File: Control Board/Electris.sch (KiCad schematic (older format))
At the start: 0 parts

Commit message: Complete schematic
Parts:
- added C1, C10, C2, C3, C7, C8, C9: 0.1uF, Capacitor_SMD:C_0603_1608Metric_Pad1.08x0.95mm_HandSolder, symbol Device:C
- added C11, C12, C4, C5: 18pF, Capacitor_SMD:C_0603_1608Metric_Pad1.08x0.95mm_HandSolder, symbol Device:C
- added C6: 47uF, Capacitor_THT:CP_Radial_D5.0mm_P2.50mm, symbol Device:CP1
- added D1: NSR0530HT1G, Diode_SMD:D_SOD-323_HandSoldering, symbol Device:D_Schottky
- added F1: 500mA, Fuse:Fuse_0603_1608Metric_Pad1.05x0.95mm_HandSolder, symbol Device:Fuse
- added FB1: Ferrite, Inductor_SMD:L_0603_1608Metric_Pad1.05x0.95mm_HandSolder, symbol Device:Ferrite_Bead_Small
- added J1: Barrel_Jack, Connector_BarrelJack:BarrelJack_Horizontal, symbol Connector:Barrel_Jack
- added J2: CTRL_ICSP, Connector_PinHeader_2.54mm:PinHeader_2x03_P2.54mm_Vertical, symbol Connector_Generic:Conn_02x03_Odd_Even
- added J3: GFX_ICSP, Connector_PinHeader_2.54mm:PinHeader_2x03_P2.54mm_Vertical, symbol Connector_Generic:Conn_02x03_Odd_Even
- added J4: VGA, jlib:Connector_Amphenol_ICD15S13E4GX00LF, symbol Connector:DB15_Female
- added JP1: CTRL_RST, Jumper:SolderJumper-2_P1.3mm_Open_RoundedPad1.0x1.5mm, symbol Device:Jumper_NC_Small
- added JP2: GFX_RST, Jumper:SolderJumper-2_P1.3mm_Open_RoundedPad1.0x1.5mm, symbol Device:Jumper_NC_Small
- added JP3: 6R, Jumper:SolderJumper-2_P1.3mm_Open_RoundedPad1.0x1.5mm, symbol Device:Jumper_NC_Small
- added JP4: 6G, Jumper:SolderJumper-2_P1.3mm_Open_RoundedPad1.0x1.5mm, symbol Device:Jumper_NC_Small
- added JP5: 6B, Jumper:SolderJumper-2_P1.3mm_Open_RoundedPad1.0x1.5mm, symbol Device:Jumper_NO_Small
- added JP6: 7R, Jumper:SolderJumper-2_P1.3mm_Open_RoundedPad1.0x1.5mm, symbol Device:Jumper_NO_Small
- added JP7: 7G, Jumper:SolderJumper-2_P1.3mm_Open_RoundedPad1.0x1.5mm, symbol Device:Jumper_NO_Small
- added JP8: 7B, Jumper:SolderJumper-2_P1.3mm_Open_RoundedPad1.0x1.5mm, symbol Device:Jumper_NC_Small
- added JP9: TONE, Jumper:SolderJumper-3_P1.3mm_Open_RoundedPad1.0x1.5mm_NumberLabels, symbol Jumper:Jumper_3_Open
- added L1: 47uH, Inductor_SMD:L_1210_3225Metric_Pad1.42x2.65mm_HandSolder, symbol Device:L
- added LS1: Speaker, Connector_PinHeader_2.54mm:PinHeader_1x02_P2.54mm_Vertical, symbol Device:Speaker
- added Q1: MMBT2222ALT3G, Package_TO_SOT_SMD:SOT-23_Handsoldering, symbol Device:Q_NPN_BEC
- added R1, R10, R11, R12, R13, R14, R2, R8, R9: 10K, Resistor_SMD:R_0603_1608Metric_Pad0.98x0.95mm_HandSolder, symbol Device:R_US
- added R3, R4: 68, Resistor_SMD:R_0805_2012Metric_Pad1.20x1.40mm_HandSolder, symbol Device:R_US
- added R5, R6: 470, Resistor_SMD:R_0603_1608Metric_Pad0.98x0.95mm_HandSolder, symbol Device:R_US
- added R7: 1K, Resistor_SMD:R_0603_1608Metric_Pad0.98x0.95mm_HandSolder, symbol Device:R_US
- added SW1: SW_ML, Button_Switch_THT:SW_PUSH-12mm, symbol Switch:SW_Push
- added SW2: SW_MR, Button_Switch_THT:SW_PUSH-12mm, symbol Switch:SW_Push
- added SW3: SW_TL, Button_Switch_THT:SW_PUSH-12mm, symbol Switch:SW_Push
- added SW4: SW_TR, Button_Switch_THT:SW_PUSH-12mm, symbol Switch:SW_Push
- added SW5: SW_DS, Button_Switch_THT:SW_PUSH-12mm, symbol Switch:SW_Push
- added SW6: SW_DH, Button_Switch_THT:SW_PUSH-12mm, symbol Switch:SW_Push
- added SW7: SW_HL, Button_Switch_THT:SW_PUSH-12mm, symbol Switch:SW_Push
- added U1, U3: ATmega328P-AU, Package_QFP:TQFP-32_7x7mm_P0.8mm, symbol MCU_Microchip_ATmega:ATmega328P-AU
- added U2: AP1509-50SG-13, Package_SO:SOP-8_3.9x4.9mm_P1.27mm, symbol jlib:AP1509-50SG-13
- added Y1, Y2: 16MHz, Crystal:Crystal_HC49-4H_Vertical, symbol Device:Crystal
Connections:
- new net: C4.2, U1.7 (XTAL1/PB6), Y1.1
- new net: C5.2, U1.8 (XTAL2/PB7), Y1.2
- new net: C2.1, U1.20 (AREF)
- new net: D1.1 (K), L1.1, U2.2 (OUT)
- new net: C6.1, C7.1, FB1.2, L1.2
- new net: R4.2, U3.1 (PD3)
- new net: R5.2, U3.10 (PD6)
- new net: R6.2, U3.11 (PD7)
- new net: R3.2, U3.13 (PB1)
- new net: C9.1, U3.20 (AREF)
- new net: C11.2, U3.7 (XTAL1/PB6), Y2.1
- new net: C12.2, U3.8 (XTAL2/PB7), Y2.2
- new net: Q1.1 (B), R7.1
- new net: LS1.2, Q1.3 (C)
- new net: JP3.1, JP4.1, JP5.1, R5.1
- new net: JP6.1, JP7.1, JP8.1, R6.1
- new net: F1.2, J1.1
- new net +12V: C3.1, F1.1, U2.1 (VIN)
- new net +5V: C1.1, C10.1, C8.1, FB1.1, J2.2 (Pin_2), J3.2 (Pin_2), LS1.1, R1.1, R2.1, SW1.2, SW2.2, SW3.2, SW4.2, SW5.2, SW6.2, SW7.2, U1.18 (AVCC), U1.4 (VCC), U1.6 (VCC), U2.3 (FB), U3.18 (AVCC), U3.4 (VCC), U3.6 (VCC)
- new net BTN_DH: R13.1, SW6.1, U1.11 (PD7)
- new net BTN_DS: R12.1, SW5.1, U1.10 (PD6)
- new net BTN_HL: R14.1, SW7.1, U1.28 (PC5)
- new net BTN_ML: R8.1, SW1.1, U1.32 (PD2)
- new net BTN_MR: R9.1, SW2.1, U1.1 (PD3)
- new net BTN_TL: R10.1, SW3.1, U1.2 (PD4)
- new net BTN_TR: R11.1, SW4.1, U1.9 (PD5)
- new net GND: C1.2, C10.2, C11.1, C12.1, C2.2, C3.2, C4.1, C5.1, C6.2, C7.2, C8.2, C9.2, D1.2 (A), J1.2, J2.6 (Pin_6), J3.6 (Pin_6), J4.10 (P10), J4.5, J4.6, J4.7, J4.8, JP1.1, JP2.1, Q1.2 (E), R10.2, R11.2, R12.2, R13.2, R14.2, R8.2, R9.2, U1.21 (GND), U1.3 (GND), U1.5 (GND), U2.4 (SD), U2.5 (GND), U2.6 (GND), U2.7 (GND), U2.8 (GND), U3.21 (GND), U3.3 (GND), U3.5 (GND)
- new net ICSP_MISO_1: J2.1 (Pin_1), U1.16 (PB4)
- new net ICSP_MISO_2: J3.1 (Pin_1), U3.16 (PB4)
- new net ICSP_MOSI_1: J2.4 (Pin_4), U1.15 (PB3)
- new net ICSP_MOSI_2: J3.4 (Pin_4), U3.15 (PB3)
- new net ICSP_SCK_1: J2.3 (Pin_3), U1.17 (PB5)
- new net ICSP_SCK_2: J3.3 (Pin_3), U3.17 (PB5)
- new net TONE: JP9.2 (C), R7.2
- new net TONE_1: JP9.3 (B), U1.13 (PB1)
- new net TONE_2: JP9.1 (A), U3.14 (PB2)
- new net UART_RX: U1.30 (PD0), U3.30 (PD0)
- new net UART_TX: U1.31 (PD1), U3.31 (PD1)
- new net VGA_B: J4.3, JP5.2, JP8.2
- new net VGA_G: J4.2, JP4.2, JP7.2
- new net VGA_HSYNC: J4.13 (P13), R4.1
- new net VGA_R: J4.1, JP3.2, JP6.2
- new net VGA_VSYNC: J4.14 (P14), R3.1
- new net nRST_1: J2.5 (Pin_5), JP1.2, R1.2, U1.29 (~RESET~/PC6)
- new net nRST_2: J3.5 (Pin_5), JP2.2, R2.2, U3.29 (~RESET~/PC6)
- no-connect marks 0 -> 26

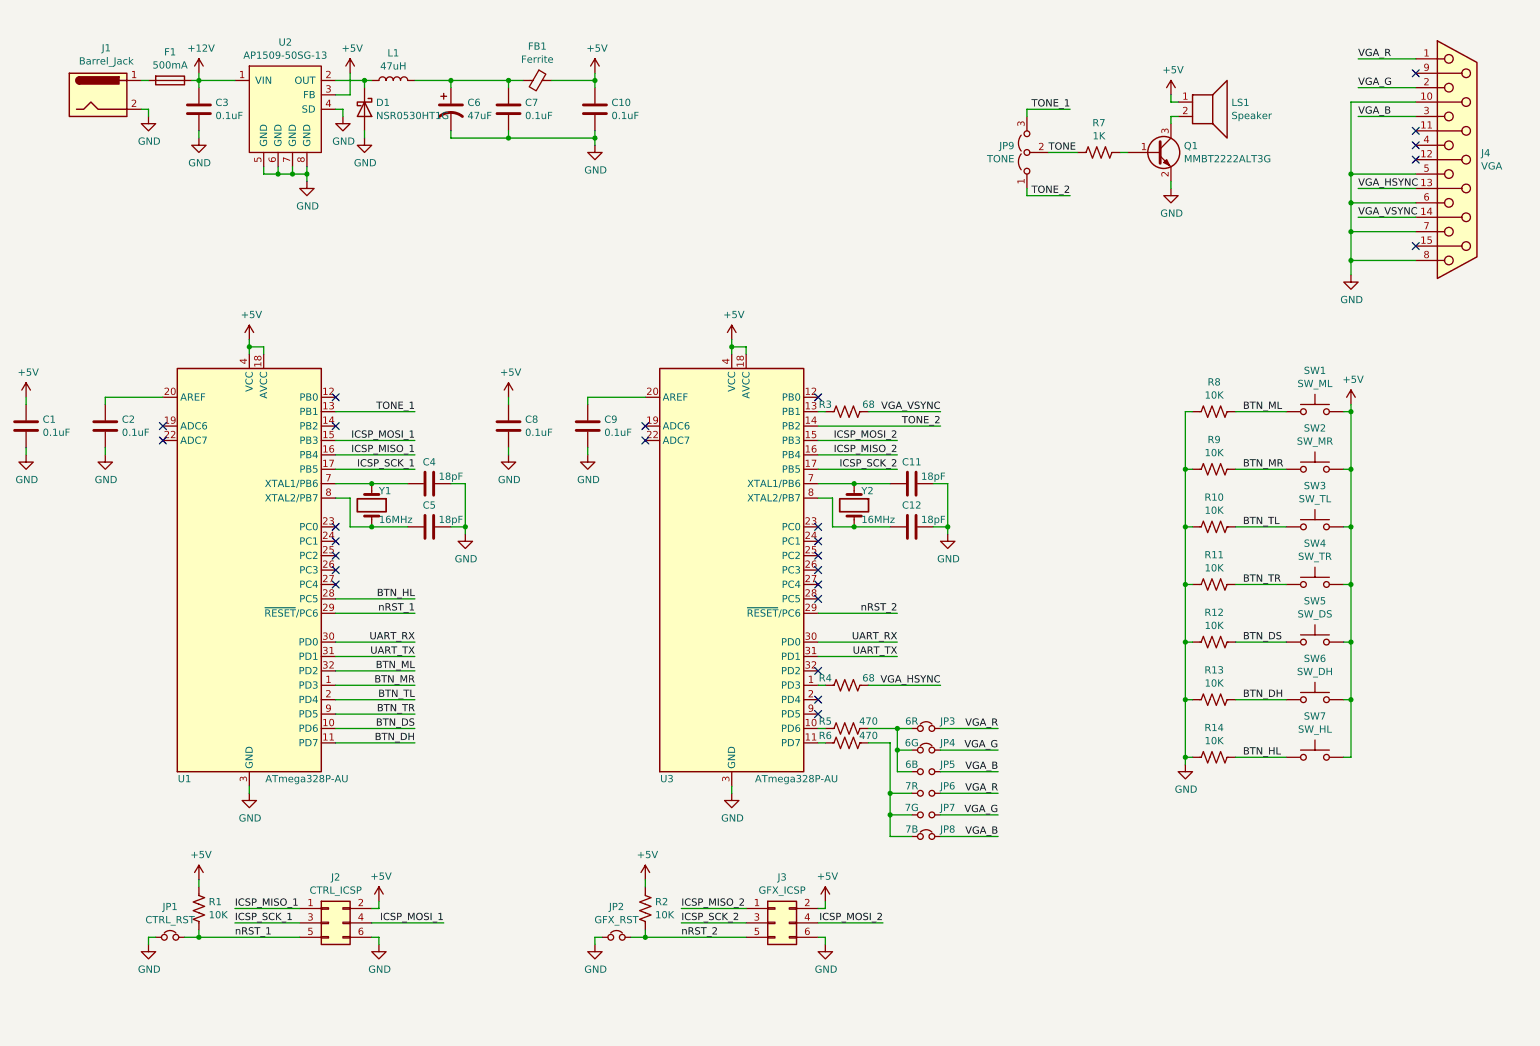
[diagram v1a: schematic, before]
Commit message: Switched to RP2040, finished schematic, started layout.
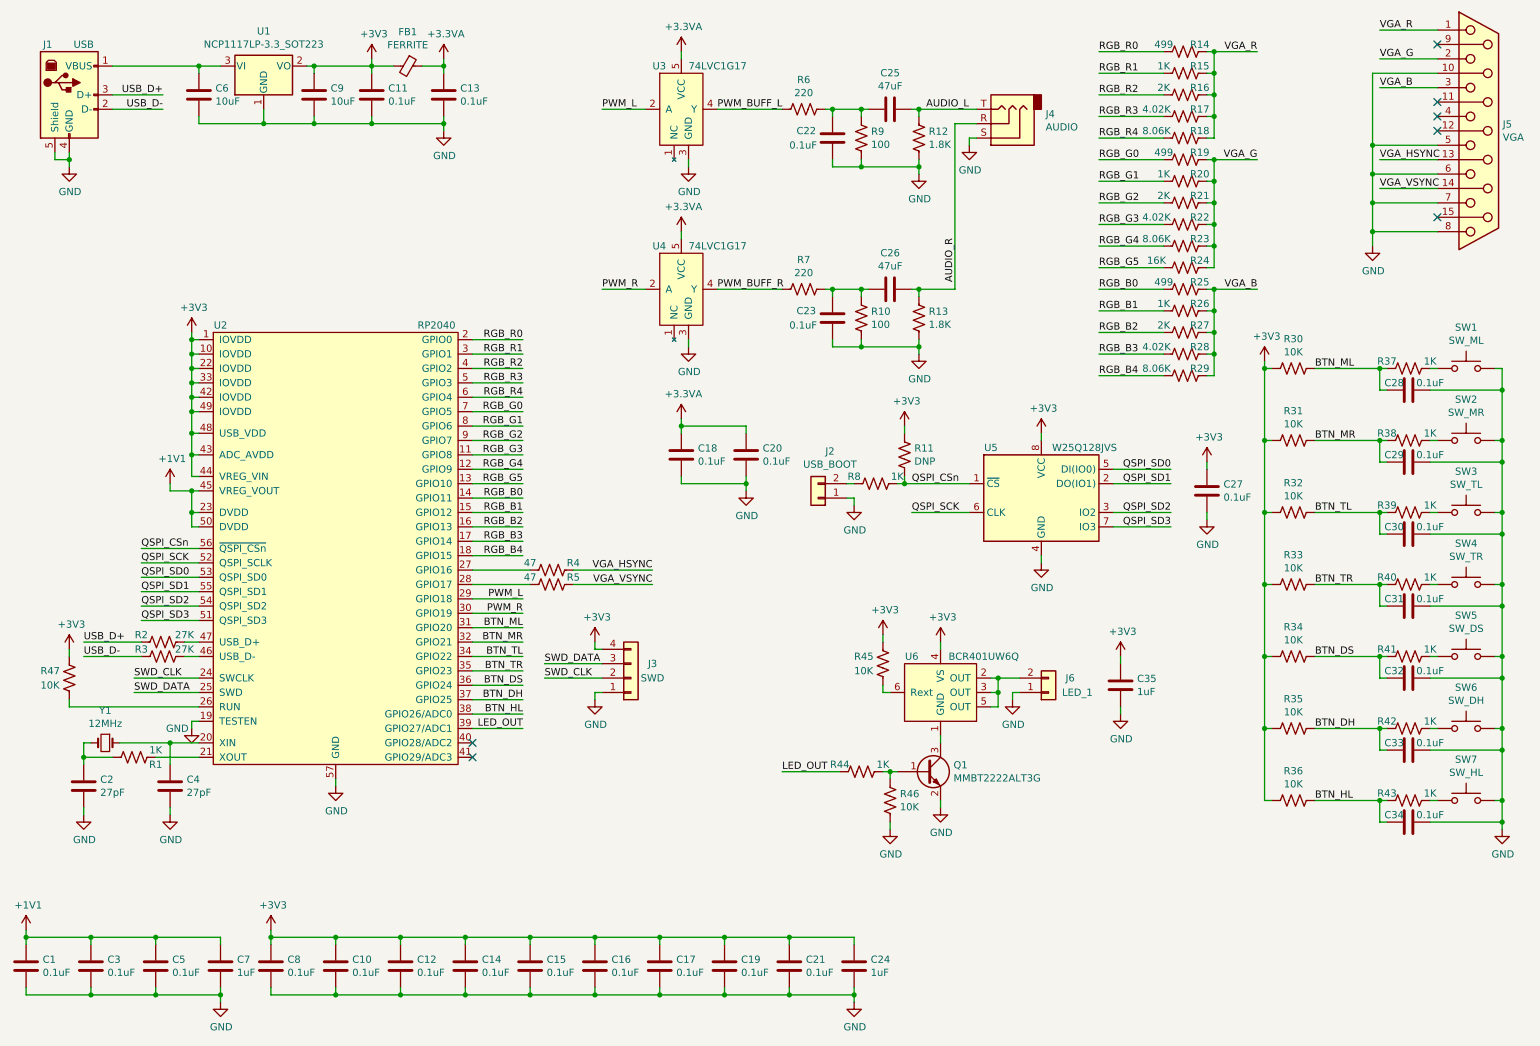
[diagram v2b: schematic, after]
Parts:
- removed C6: 47uF, Capacitor_THT:CP_Radial_D5.0mm_P2.50mm, symbol Device:CP1
- removed D1: NSR0530HT1G, Diode_SMD:D_SOD-323_HandSoldering, symbol Device:D_Schottky
- removed F1: 500mA, Fuse:Fuse_0603_1608Metric_Pad1.05x0.95mm_HandSolder, symbol Device:Fuse
- removed J1: Barrel_Jack, Connector_BarrelJack:BarrelJack_Horizontal, symbol Connector:Barrel_Jack
- removed J2: CTRL_ICSP, Connector_PinHeader_2.54mm:PinHeader_2x03_P2.54mm_Vertical, symbol Connector_Generic:Conn_02x03_Odd_Even
- removed J3: GFX_ICSP, Connector_PinHeader_2.54mm:PinHeader_2x03_P2.54mm_Vertical, symbol Connector_Generic:Conn_02x03_Odd_Even
- removed JP1: CTRL_RST, Jumper:SolderJumper-2_P1.3mm_Open_RoundedPad1.0x1.5mm, symbol Device:Jumper_NC_Small
- removed JP2: GFX_RST, Jumper:SolderJumper-2_P1.3mm_Open_RoundedPad1.0x1.5mm, symbol Device:Jumper_NC_Small
- removed JP3: 6R, Jumper:SolderJumper-2_P1.3mm_Open_RoundedPad1.0x1.5mm, symbol Device:Jumper_NC_Small
- removed JP4: 6G, Jumper:SolderJumper-2_P1.3mm_Open_RoundedPad1.0x1.5mm, symbol Device:Jumper_NC_Small
- removed JP5: 6B, Jumper:SolderJumper-2_P1.3mm_Open_RoundedPad1.0x1.5mm, symbol Device:Jumper_NO_Small
- removed JP6: 7R, Jumper:SolderJumper-2_P1.3mm_Open_RoundedPad1.0x1.5mm, symbol Device:Jumper_NO_Small
- removed JP7: 7G, Jumper:SolderJumper-2_P1.3mm_Open_RoundedPad1.0x1.5mm, symbol Device:Jumper_NO_Small
- removed JP8: 7B, Jumper:SolderJumper-2_P1.3mm_Open_RoundedPad1.0x1.5mm, symbol Device:Jumper_NC_Small
- removed JP9: TONE, Jumper:SolderJumper-3_P1.3mm_Open_RoundedPad1.0x1.5mm_NumberLabels, symbol Jumper:Jumper_3_Open
- removed L1: 47uH, Inductor_SMD:L_1210_3225Metric_Pad1.42x2.65mm_HandSolder, symbol Device:L
- removed LS1: Speaker, Connector_PinHeader_2.54mm:PinHeader_1x02_P2.54mm_Vertical, symbol Device:Speaker
- removed U1, U3: ATmega328P-AU, Package_QFP:TQFP-32_7x7mm_P0.8mm, symbol MCU_Microchip_ATmega:ATmega328P-AU
- removed U2: AP1509-50SG-13, Package_SO:SOP-8_3.9x4.9mm_P1.27mm, symbol jlib:AP1509-50SG-13
- removed Y1, Y2: 16MHz, Crystal:Crystal_HC49-4H_Vertical, symbol Device:Crystal
- added C13, C14, C15, C16, C17, C18, C19, C20, C21, C22, C23, C27, C28, C29, C30, C31, C32, C33, C34: 0.1uF, Capacitor_SMD:C_0603_1608Metric_Pad1.08x0.95mm_HandSolder, symbol Device:C
- added C24, C35: 1uF, Capacitor_SMD:C_0603_1608Metric_Pad1.08x0.95mm_HandSolder, symbol Device:C
- added C25, C26: 47uF, Capacitor_SMD:C_0805_2012Metric_Pad1.18x1.45mm_HandSolder, symbol Device:C
- added C6: 10uF, Capacitor_SMD:C_0805_2012Metric_Pad1.18x1.45mm_HandSolder, symbol Device:C
- added J1: USB, Connector_USB:USB_B_OST_USB-B1HSxx_Horizontal, symbol Connector:USB_B
- added J2: USB_BOOT, Jumper:SolderJumper-2_P1.3mm_Open_RoundedPad1.0x1.5mm, symbol Connector_Generic:Conn_01x02
- added J3: SWD, Connector_PinHeader_2.54mm:PinHeader_1x04_P2.54mm_Vertical, symbol Connector_Generic:Conn_01x04
- added J4: AUDIO, jlib:Connector_CUI_SJ1-2503A, symbol Connector:AudioJack3
- added J6: LED_1, Connector_JST:JST_EH_B2B-EH-A_1x02_P2.50mm_Vertical, symbol Connector_Generic:Conn_01x02
- added R10, R9: 100, Resistor_SMD:R_0805_2012Metric_Pad1.20x1.40mm_HandSolder, symbol Device:R_US
- added R11: DNP, Resistor_SMD:R_0603_1608Metric_Pad0.98x0.95mm_HandSolder, symbol Device:R_US
- added R12, R13: 1.8K, Resistor_SMD:R_0805_2012Metric_Pad1.20x1.40mm_HandSolder, symbol Device:R_US
- added R14, R19, R25: 499, Resistor_SMD:R_0603_1608Metric_Pad0.98x0.95mm_HandSolder, symbol Device:R_US
- added R15, R20, R26, R37, R38, R39, R40, R41, R42, R43, R44, R8: 1K, Resistor_SMD:R_0603_1608Metric_Pad0.98x0.95mm_HandSolder, symbol Device:R_US
- added R16, R21, R27: 2K, Resistor_SMD:R_0603_1608Metric_Pad0.98x0.95mm_HandSolder, symbol Device:R_US
- added R17, R22, R28: 4.02K, Resistor_SMD:R_0603_1608Metric_Pad0.98x0.95mm_HandSolder, symbol Device:R_US
- added R18, R23, R29: 8.06K, Resistor_SMD:R_0603_1608Metric_Pad0.98x0.95mm_HandSolder, symbol Device:R_US
- added R24: 16K, Resistor_SMD:R_0603_1608Metric_Pad0.98x0.95mm_HandSolder, symbol Device:R_US
- added R45, R46, R47: 10K, Resistor_SMD:R_0603_1608Metric_Pad0.98x0.95mm_HandSolder, symbol Device:R_US
- added U1: NCP1117LP-3.3_SOT223, Package_TO_SOT_SMD:SOT-223-3_TabPin2, symbol Regulator_Linear:NCP1117-3.3_SOT223
- added U2: RP2040, jlib:QFN_RP2040, symbol jlib:RP2040
- added U3, U4: 74LVC1G17, Package_TO_SOT_SMD:TSOT-23-5_HandSoldering, symbol jlib:74LVC1G17
- added U5: W25Q128JVS, Package_SO:SOIC-8_5.23x5.23mm_P1.27mm, symbol Memory_Flash:W25Q128JVS
- added U6: BCR401UW6Q, Package_TO_SOT_SMD:SOT-23-6_Handsoldering, symbol jlib:BCR401UW6Q
- added Y1: 12MHz, Crystal:Crystal_SMD_HC49-SD, symbol Device:Crystal_Small
- C11, C12, C5: value 18pF -> 0.1uF
- C2: value 0.1uF -> 27pF
- C4: value 18pF -> 27pF
- C7: value 0.1uF -> 1uF
- C9: value 0.1uF -> 10uF; footprint Capacitor_SMD:C_0603_1608Metric_Pad1.08x0.95mm_HandSolder -> Capacitor_SMD:C_0805_2012Metric_Pad1.18x1.45mm_HandSolder
- FB1: value Ferrite -> FERRITE
- Q1: footprint Package_TO_SOT_SMD:SOT-23_Handsoldering -> Package_TO_SOT_SMD:TSOT-23_HandSoldering
- R1: value 10K -> 1K
- R2: value 10K -> 27K; footprint Resistor_SMD:R_0603_1608Metric_Pad0.98x0.95mm_HandSolder -> Resistor_SMD:R_0805_2012Metric_Pad1.20x1.40mm_HandSolder
- R3: value 68 -> 27K
- R4: value 68 -> 47; footprint Resistor_SMD:R_0805_2012Metric_Pad1.20x1.40mm_HandSolder -> Resistor_SMD:R_0603_1608Metric_Pad0.98x0.95mm_HandSolder
- R5: value 470 -> 47
- R6: value 470 -> 220; footprint Resistor_SMD:R_0603_1608Metric_Pad0.98x0.95mm_HandSolder -> Resistor_SMD:R_0805_2012Metric_Pad1.20x1.40mm_HandSolder
- R7: value 1K -> 220; footprint Resistor_SMD:R_0603_1608Metric_Pad0.98x0.95mm_HandSolder -> Resistor_SMD:R_0805_2012Metric_Pad1.20x1.40mm_HandSolder
- SW1, SW2, SW3, SW4, SW5, SW6, SW7: footprint Button_Switch_THT:SW_PUSH-12mm -> Connector_JST:JST_EH_B2B-EH-A_1x02_P2.50mm_Vertical
- renumbered J4 to J5, R8 to R30, R9 to R31, R10 to R32, R11 to R33, R12 to R34, R13 to R35, R14 to R36
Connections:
- net +12V is gone; now on net +1V1: C3.1
- net nRST_1 is gone; now on an unnamed net: R1.2
- net BTN_DH: now also C33.2, R42.2, U2.37 (GPIO25); no longer SW6.1
- net BTN_DS: now also C32.2, R41.2, U2.36 (GPIO24); no longer SW5.1
- net BTN_HL: now also C34.2, R43.2, U2.38 (GPIO26/ADC0); no longer SW7.1
- net BTN_ML: now also C28.2, R37.2, U2.31 (GPIO20); no longer SW1.1
- net BTN_MR: now also C29.2, R38.2, U2.32 (GPIO21); no longer SW2.1
- net BTN_TL: now also C30.2, R39.2, U2.34 (GPIO22); no longer SW3.1
- net BTN_TR: now also C31.2, R40.2, U2.35 (GPIO23); no longer SW4.1
- net GND: now also C11.2, C12.2, C4.2, C5.2, SW1.2, SW2.2, SW3.2, SW4.2, SW5.2, SW6.2, SW7.2, C13.2, C14.2, C15.2, C16.2, C17.2, C18.2, C19.2, C20.2, C21.2, C22.2, C23.2, C24.2, C27.2, C28.1, C29.1, C30.1, C31.1, C32.1, C33.1, C34.1, C35.2, C6.2, J1.4 (GND), J1.5 (Shield), J2.1 (Pin_1), J3.1 (Pin_1), J4.S, J6.1 (Pin_1), R10.2, R12.2, R13.2, R46.2, R9.2, U1.1 (GND), U2.19 (TESTEN), U2.57 (GND), U3.3 (GND), U4.3 (GND), U5.4 (GND); no longer C11.1, C12.1, C4.1, C5.1, R30.2, R31.2, R32.2, R33.2, R34.2, R35.2, R36.2
- net VGA_B: now also R25.1, R26.1, R27.1, R28.1, R29.1
- net VGA_G: now also R19.1, R20.1, R21.1, R22.1, R23.1, R24.1
- net VGA_R: now also R14.1, R15.1, R16.1, R17.1, R18.1
- net VGA_VSYNC: now also R5.1; no longer R3.1
- net at C2.1: now also Y1.2
- net +1V1: now reaches C7.1
- net +1V1: now also C1.1, C5.1, U2.23 (DVDD), U2.45 (VREG_VOUT), U2.50 (DVDD); no longer FB1.2
- net at R4.2: now also U2.27 (GPIO16)
- net at R5.2: now also U2.28 (GPIO17)
- net PWM_BUFF_L: now reaches R6.2
- net PWM_BUFF_L: now also U3.4 (Y)
- net USB_D-: now reaches R3.2
- net USB_D-: now also J1.2 (D-)
- net +3V3: now reaches C9.1
- net +3V3: now also C10.1, C11.1, C12.1, C8.1, FB1.2, R30.2, R31.2, R32.2, R33.2, R34.2, R35.2, R36.2, C14.1, C15.1, C16.1, C17.1, C19.1, C21.1, C24.1, C27.1, C35.1, J3.4 (Pin_4), R11.1, R45.1, R47.1, U1.2 (VO), U2.1 (IOVDD), U2.10 (IOVDD), U2.22 (IOVDD), U2.33 (IOVDD), U2.42 (IOVDD), U2.43 (ADC_AVDD), U2.44 (VREG_VIN), U2.48 (USB_VDD), U2.49 (IOVDD), U5.8 (VCC), U6.4 (VS)
- net at Q1.1 (B): now also R44.1, R46.1; no longer R7.1
- net at Q1.3 (C): now also U6.1 (GND)
- net at R6.1: now also C22.1, C25.2, R9.1
- removed net +5V: C1.1, C10.1, C8.1, FB1.1, R1.1, R2.1, SW1.2, SW2.2, SW3.2, SW4.2, SW5.2, SW6.2, SW7.2
- net TONE renamed PWM_BUFF_R
- net PWM_BUFF_R: now also U4.4 (Y)
- net nRST_2 renamed USB_D+
- net USB_D+: now also J1.3 (D+)
- new net: R40.1, SW4.1
- new net: R41.1, SW5.1
- new net: R42.1, SW6.1
- new net: R43.1, SW7.1
- new net: R37.1, SW1.1
- new net: R38.1, SW2.1
- new net: R39.1, SW3.1
- new net: C4.1, U2.20 (XIN), Y1.1
- new net: R1.1, U2.21 (XOUT)
- new net: R47.2, U2.26 (RUN)
- new net: R3.1, U2.46 (USB_D-)
- new net: R2.1, U2.47 (USB_D+)
- new net: J6.2 (Pin_2), U6.2 (OUT), U6.3 (OUT), U6.5 (OUT)
- new net: R45.2, U6.6 (Rext)
- new net: J2.2 (Pin_2), R8.2
- new net: C6.1, J1.1 (VBUS), U1.3 (VI)
- new net: C23.1, C26.2, R10.1, R7.1
- new net +3.3VA: C13.1, C18.1, C20.1, FB1.1, U3.5 (VCC), U4.5 (VCC)
- new net AUDIO_L: C25.1, J4.T, R12.1
- new net AUDIO_R: C26.1, J4.R, R13.1
- new net LED_OUT: R44.2, U2.39 (GPIO27/ADC1)
- new net PWM_L: U2.29 (GPIO18), U3.2 (A)
- new net PWM_R: U2.30 (GPIO19), U4.2 (A)
- new net QSPI_CSn: R11.2, R8.1, U2.56 (~QSPI_CSn~), U5.1 (~CS)
- new net QSPI_SCK: U2.52 (QSPI_SCLK), U5.6 (CLK)
- new net QSPI_SD0: U2.53 (QSPI_SD0), U5.5 (DI(IO0))
- new net QSPI_SD1: U2.55 (QSPI_SD1), U5.2 (DO(IO1))
- new net QSPI_SD2: U2.54 (QSPI_SD2), U5.3 (IO2)
- new net QSPI_SD3: U2.51 (QSPI_SD3), U5.7 (IO3)
- new net RGB_B0: R25.2, U2.14 (GPIO11)
- new net RGB_B1: R26.2, U2.15 (GPIO12)
- new net RGB_B2: R27.2, U2.16 (GPIO13)
- new net RGB_B3: R28.2, U2.17 (GPIO14)
- new net RGB_B4: R29.2, U2.18 (GPIO15)
- new net RGB_G0: R19.2, U2.7 (GPIO5)
- new net RGB_G1: R20.2, U2.8 (GPIO6)
- new net RGB_G2: R21.2, U2.9 (GPIO7)
- new net RGB_G3: R22.2, U2.11 (GPIO8)
- new net RGB_G4: R23.2, U2.12 (GPIO9)
- new net RGB_G5: R24.2, U2.13 (GPIO10)
- new net RGB_R0: R14.2, U2.2 (GPIO0)
- new net RGB_R1: R15.2, U2.3 (GPIO1)
- new net RGB_R2: R16.2, U2.4 (GPIO2)
- new net RGB_R3: R17.2, U2.5 (GPIO3)
- new net RGB_R4: R18.2, U2.6 (GPIO4)
- new net SWD_CLK: J3.2 (Pin_2), U2.24 (SWCLK)
- new net SWD_DATA: J3.3 (Pin_3), U2.25 (SWD)
- no-connect marks 26 -> 7
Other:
- moved on the sheet: J5, R30, R31, R32, R33, R34, R35, R36, SW1, SW2, SW3, SW4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

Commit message: Routing
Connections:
- net D-: now reaches R3.1, U2.46 (USB_D-)
- net D+: now reaches R2.1, U2.47 (USB_D+)
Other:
- moved on the sheet: R2, R3, R47
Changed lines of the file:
@@
 Text Label 7150 2450 1    50   ~ 0
 AUDIO_R
-Text Label 1450 5200 0    50   ~ 0
+Text Label 1300 5200 0    50   ~ 0
 SWD_CLK
 Wire Wire Line
-	1450 5200 1900 5200
-Wire Wire Line
-	1450 5300 1900 5300
-Text Label 1450 5300 0    50   ~ 0
+	1300 5200 1900 5200
+Wire Wire Line
+	1300 5300 1900 5300
+Text Label 1300 5300 0    50   ~ 0
 SWD_DATA
 $Comp
@@
 L Device:R_US R2
 U 1 1 614243B8
-P 1650 4950
-F 0 "R2" V 1600 4800 50  0000 C CNN
-F 1 "27K" V 1600 5100 50  0000 C CNN
-F 2 "Resistor_SMD:R_0805_2012Metric_Pad1.20x1.40mm_HandSolder" V 1690 4940 50  0001 C CNN
-F 3 "~" H 1650 4950 50  0001 C CNN
-	1    1650 4950
-	0    1    1    0
-$EndComp
-Wire Wire Line
-	1800 4950 1900 4950
-Wire Wire Line
-	1900 5050 1800 5050
+P 1500 4950
+F 0 "R2" V 1450 4800 50  0000 C CNN
+F 1 "27K" V 1450 5100 50  0000 C CNN
+F 2 "Resistor_SMD:R_0805_2012Metric_Pad1.20x1.40mm_HandSolder" V 1540 4940 50  0001 C CNN
+F 3 "~" H 1500 4950 50  0001 C CNN
+	1    1500 4950
+	0    1    1    0
+$EndComp
+Wire Wire Line
+	1650 4950 1900 4950
+Wire Wire Line
+	1900 5050 1650 5050
 $Comp
 L Device:R_US R3
 U 1 1 61459653
-P 1650 5050
-F 0 "R3" V 1600 4900 50  0000 C CNN
-F 1 "27K" V 1600 5200 50  0000 C CNN
-F 2 "Resistor_SMD:R_0805_2012Metric_Pad1.20x1.40mm_HandSolder" V 1690 5040 50  0001 C CNN
-F 3 "~" H 1650 5050 50  0001 C CNN
-	1    1650 5050
-	0    1    1    0
-$EndComp
-Wire Wire Line
-	1500 4950 1100 4950
-Wire Wire Line
-	1100 5050 1500 5050
-Text Label 1100 4950 0    50   ~ 0
+P 1500 5050
+F 0 "R3" V 1450 4900 50  0000 C CNN
+F 1 "27K" V 1450 5200 50  0000 C CNN
+F 2 "Resistor_SMD:R_0805_2012Metric_Pad1.20x1.40mm_HandSolder" V 1540 5040 50  0001 C CNN
+F 3 "~" H 1500 5050 50  0001 C CNN
+	1    1500 5050
+	0    1    1    0
+$EndComp
+Wire Wire Line
+	1350 4950 950  4950
+Wire Wire Line
+	950  5050 1350 5050
+Text Label 950  4950 0    50   ~ 0
 USB_D+
-Text Label 1100 5050 0    50   ~ 0
+Text Label 950  5050 0    50   ~ 0
 USB_D-
 $Comp
@@
 L Device:R_US R47
 U 1 1 61BCC099
-P 1000 5200
-F 0 "R47" H 800 5250 50  0000 L CNN
-F 1 "10K" H 800 5150 50  0000 L CNN
-F 2 "Resistor_SMD:R_0603_1608Metric_Pad0.98x0.95mm_HandSolder" V 1040 5190 50  0001 C CNN
-F 3 "~" H 1000 5200 50  0001 C CNN
-	1    1000 5200
-	1    0    0    -1
-$EndComp
-Wire Wire Line
-	1900 5400 1000 5400
-Wire Wire Line
-	1000 5400 1000 5350
-Wire Wire Line
-	1000 5050 1000 5000
+P 850 5200
+F 0 "R47" H 650 5250 50  0000 L CNN
+F 1 "10K" H 650 5150 50  0000 L CNN
+F 2 "Resistor_SMD:R_0603_1608Metric_Pad0.98x0.95mm_HandSolder" V 890 5190 50  0001 C CNN
+F 3 "~" H 850 5200 50  0001 C CNN
+	1    850  5200
+	1    0    0    -1
+$EndComp
+Wire Wire Line
+	1900 5400 850  5400
+Wire Wire Line
+	850  5400 850  5350
+Wire Wire Line
+	850  5050 850  5000
 $Comp
 L power:+3V3 #PWR041
 U 1 1 61C8940C
-P 1000 5000
-F 0 "#PWR041" H 1000 4850 50  0001 C CNN
-F 1 "+3V3" H 1015 5173 50  0000 C CNN
-F 2 "" H 1000 5000 50  0001 C CNN
-F 3 "" H 1000 5000 50  0001 C CNN
-	1    1000 5000
-	1    0    0    -1
-$EndComp
+P 850 5000
+F 0 "#PWR041" H 850 4850 50  0001 C CNN
+F 1 "+3V3" H 865 5173 50  0000 C CNN
+F 2 "" H 850 5000 50  0001 C CNN
+F 3 "" H 850 5000 50  0001 C CNN
+	1    850  5000
+	1    0    0    -1
+$EndComp
+Text Label 1750 4950 0    50   ~ 0
+D+
+Text Label 1750 5050 0    50   ~ 0
+D-
 $EndSCHEMATC

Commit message: Board ready for production
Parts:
- R2, R3: value 27K -> 27
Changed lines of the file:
@@
 P 1500 4950
 F 0 "R2" V 1450 4800 50  0000 C CNN
-F 1 "27K" V 1450 5100 50  0000 C CNN
+F 1 "27" V 1450 5100 50  0000 C CNN
 F 2 "Resistor_SMD:R_0805_2012Metric_Pad1.20x1.40mm_HandSolder" V 1540 4940 50  0001 C CNN
 F 3 "~" H 1500 4950 50  0001 C CNN
@@
 P 1500 5050
 F 0 "R3" V 1450 4900 50  0000 C CNN
-F 1 "27K" V 1450 5200 50  0000 C CNN
+F 1 "27" V 1450 5200 50  0000 C CNN
 F 2 "Resistor_SMD:R_0805_2012Metric_Pad1.20x1.40mm_HandSolder" V 1540 5040 50  0001 C CNN
 F 3 "~" H 1500 5050 50  0001 C CNN
